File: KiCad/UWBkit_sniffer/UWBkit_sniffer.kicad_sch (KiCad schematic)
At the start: 10 parts, among them J10 Conn_SPIM, J4 Conn_01x04, J5 Conn_I2C2, J8 Conn_SPIS, J9 Conn_I2C1, SW2 SW_Slide_DPDT

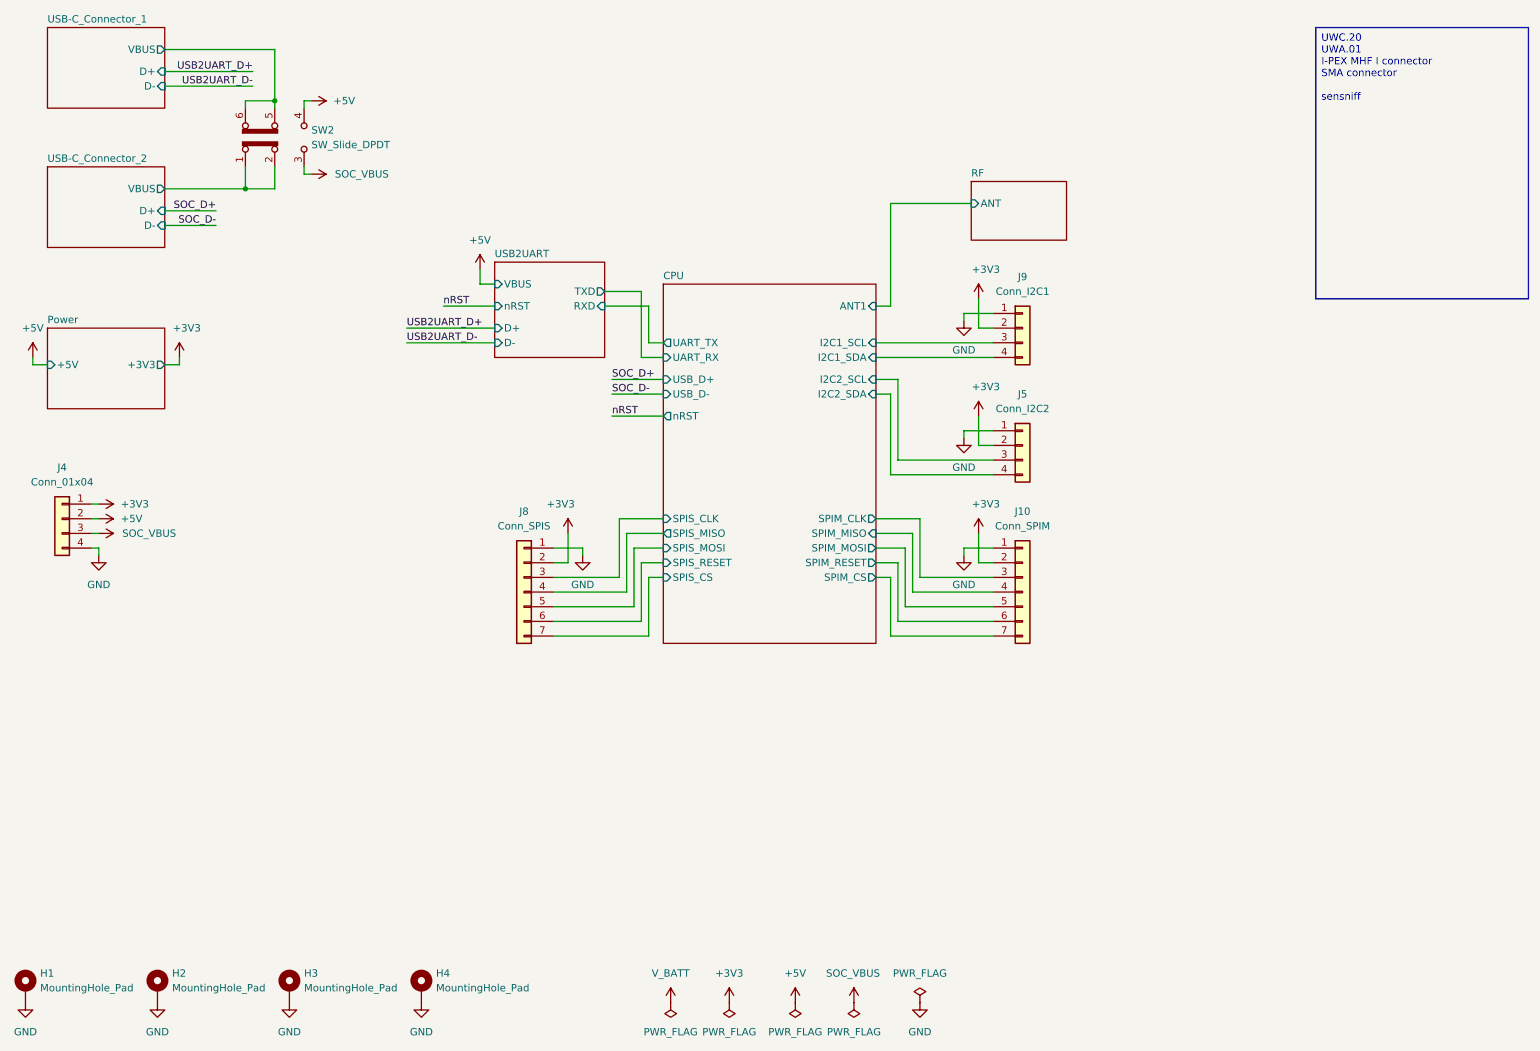
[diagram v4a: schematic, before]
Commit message: United 5V rails, modified layout of connectors
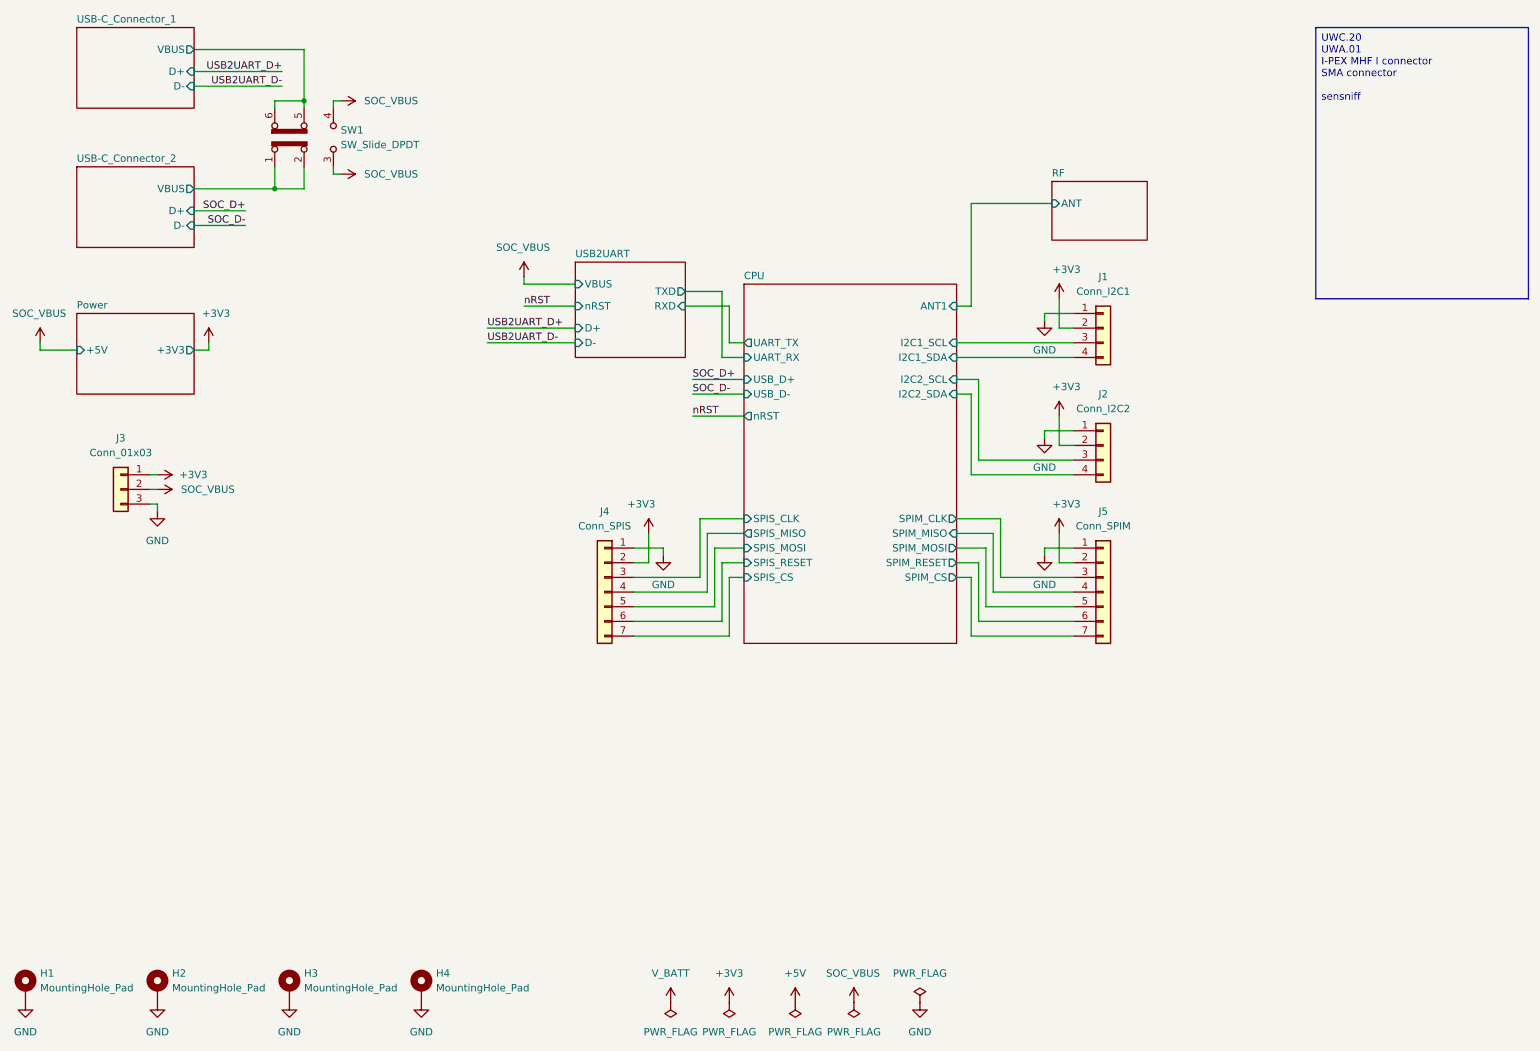
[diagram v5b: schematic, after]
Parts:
- removed J4: Conn_01x04, Connector_PinHeader_2.54mm:PinHeader_1x04_P2.54mm_Vertical, symbol Connector_Generic:Conn_01x04
- added J3: Conn_01x03, Connector_PinSocket_2.54mm:PinSocket_1x03_P2.54mm_Vertical, symbol Connector_Generic:Conn_01x03
- renumbered J9 to J1, J5 to J2, J8 to J4, J10 to J5, SW2 to SW1
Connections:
- net +3V3: now also J3.1 (Pin_1)
- net +5V: no longer SW1.4 (A)
- net GND: now also J3.3 (Pin_3)
- net SOC_VBUS: now also SW1.4 (A), J3.2 (Pin_2)
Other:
- moved on the sheet: J1, J2, J4, J5, SW1

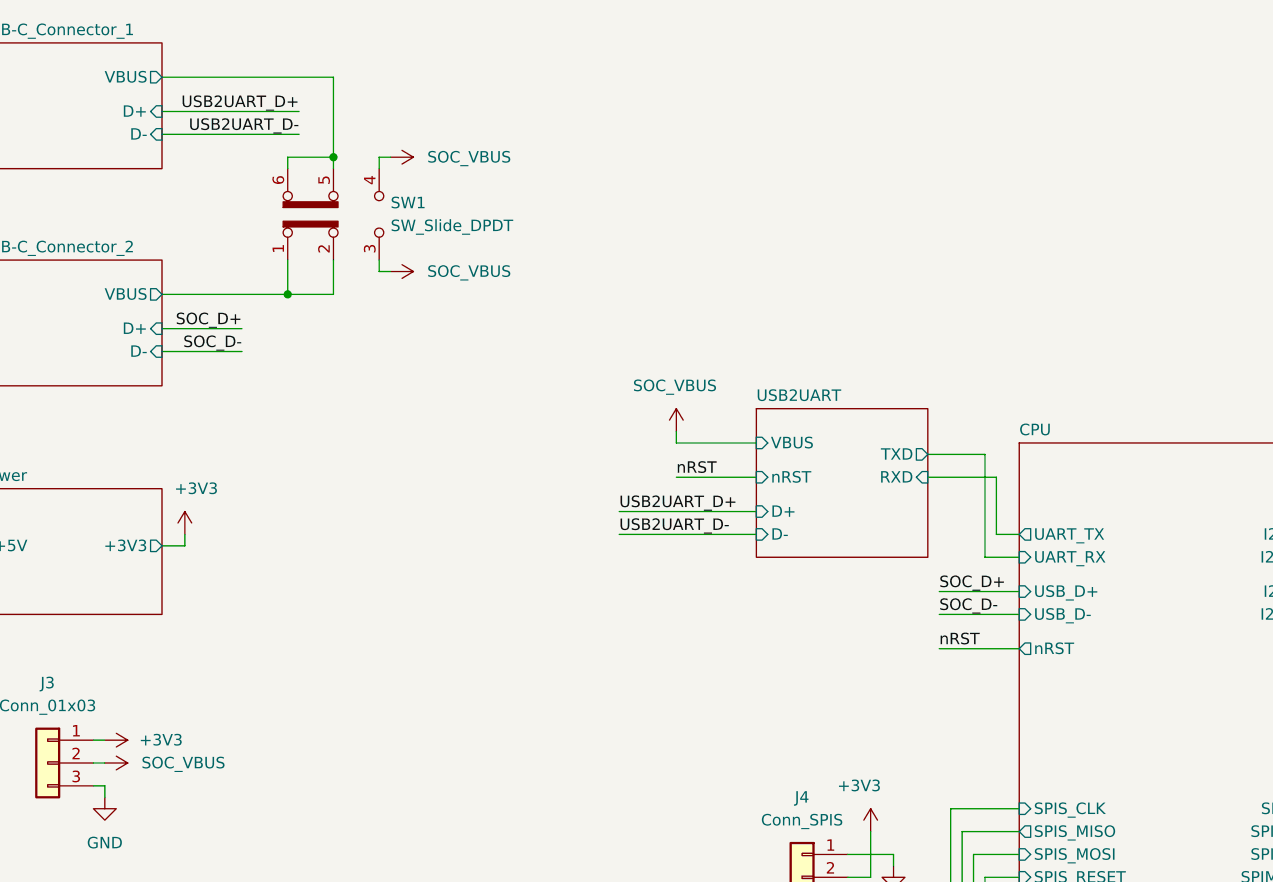
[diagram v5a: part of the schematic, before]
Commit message: Removed UWA.01, added CTS/RTS connections
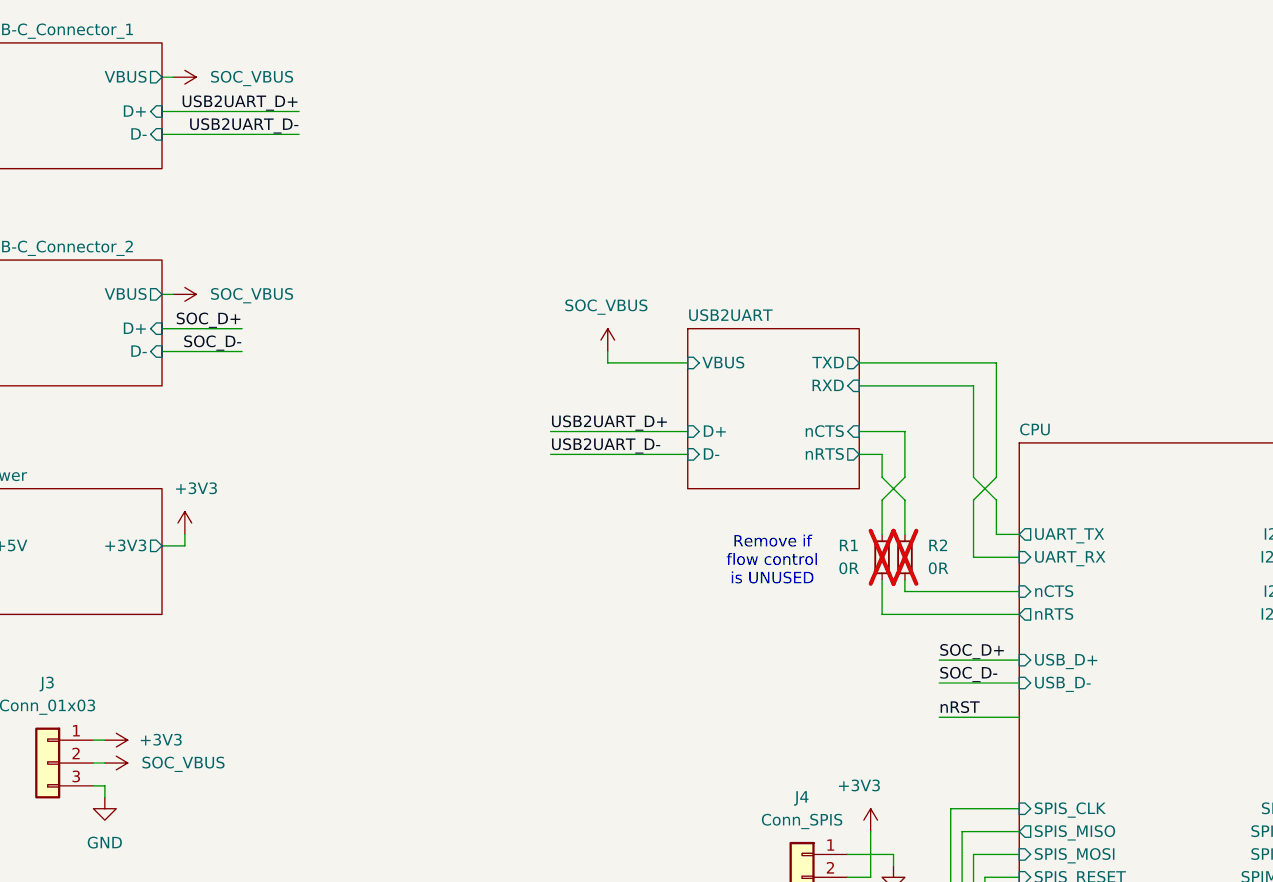
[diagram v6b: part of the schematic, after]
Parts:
- removed SW1: SW_Slide_DPDT, Button_Switch_THT:SW_CK_JS202011CQN_DPDT_Straight, symbol Switch:SW_Slide_DPDT
- added R1, R2: 0R, Resistor_SMD:R_0603_1608Metric, symbol Device:R_Small
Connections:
- new net CPU/nCTS: R2.2
- new net CPU/nRTS: R1.2
- new net USB2UART/nCTS: R1.1
- new net USB2UART/nRTS: R2.1
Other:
- sheet CPU ports: added nCTS, nRTS; removed nRST
- sheet USB2UART ports: added nCTS, nRTS; removed nRST
- note added: "Remove if flow control is UNUSED"

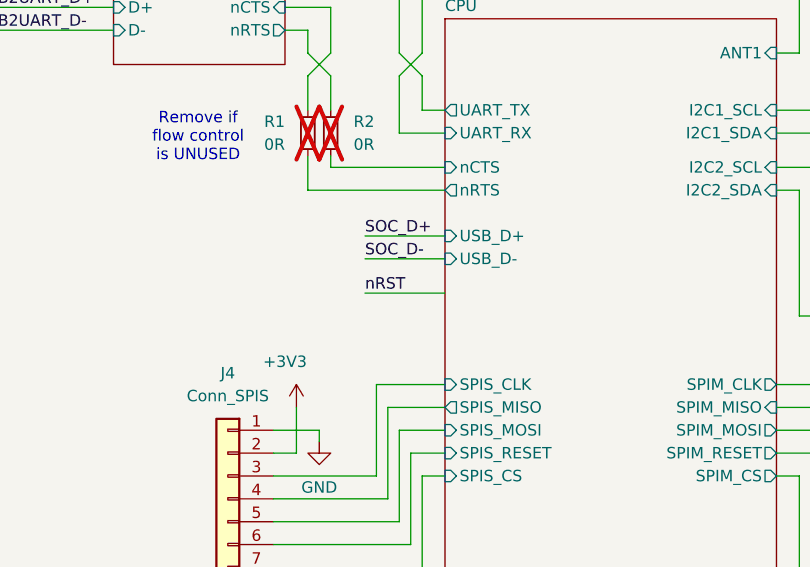
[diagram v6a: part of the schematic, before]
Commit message: Redone RF trace, repositioned UWC.20 and mounting holes
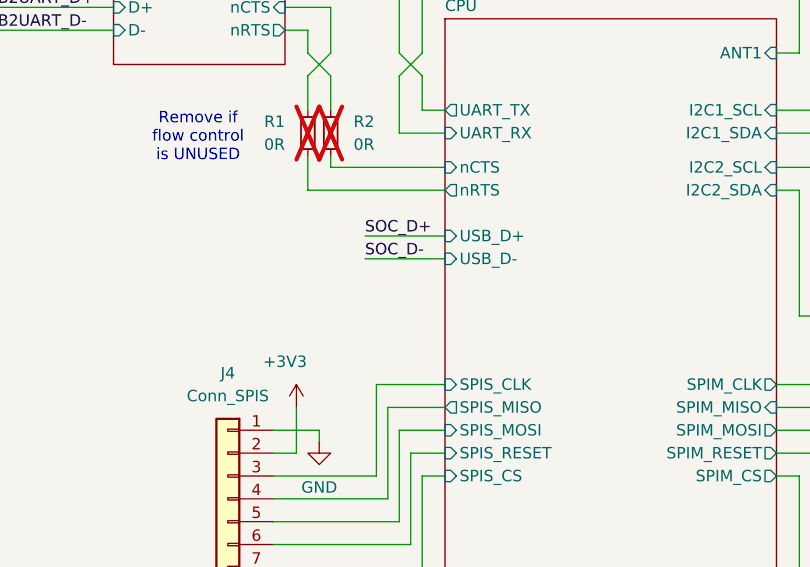
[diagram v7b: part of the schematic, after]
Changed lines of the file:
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@@
-	(wire
-		(pts
-			(xy 132.08 93.98) (xy 140.97 93.98)
-		)
-		(stroke
-			(width 0)
-			(type default)
-		)
-	)
 	(wire
 		(pts
@@
 		)
 	)
-	(label "nRST"
-		(at 132.08 93.98 0)
-		(effects
-			(font
-				(size 1.27 1.27)
-			)
-			(justify left bottom)
-		)
-	)
